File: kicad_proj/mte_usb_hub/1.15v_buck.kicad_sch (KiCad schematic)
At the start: 11 parts

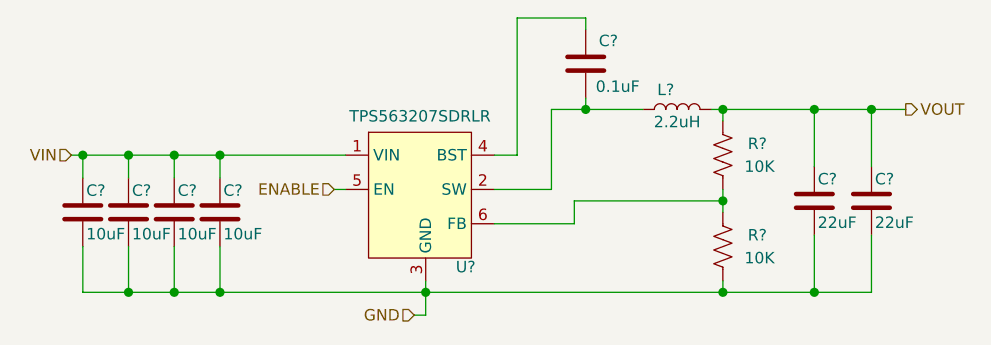
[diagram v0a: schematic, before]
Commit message: Finishes input filter, minor buck changes
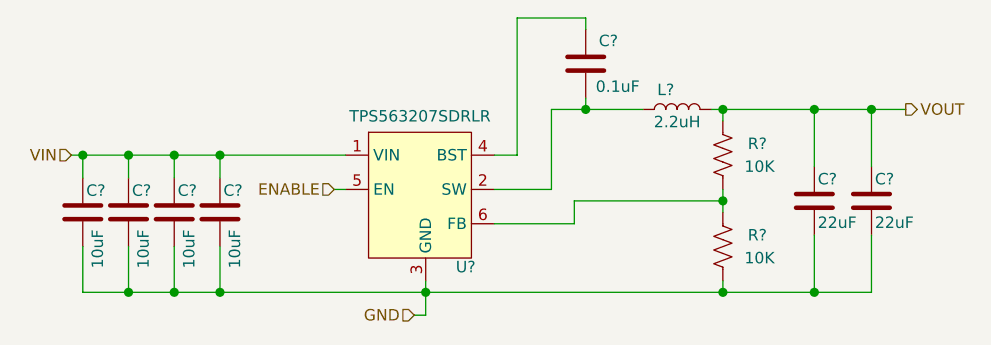
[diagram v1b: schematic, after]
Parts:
- removed C? (x4): C1608X5R1E106M080AC, footprints:CAPACITOR_0603N, symbol mte_usb_hub:C1608X5R1E106M080AC
- added C? (x4): GRM31CR71E106KA12L, footprints:CAPACITOR_1206N, symbol mte_usb_hub:GRM31CR71E106KA12L
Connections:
- net GND: now also C?.2, C?.2, C?.2, C?.2
- net VIN: now also C?.1, C?.1, C?.1, C?.1
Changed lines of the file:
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@@
     (pin "2")
   )
-  (symbol (lib_id "mte_usb_hub:C1608X5R1E106M080AC") (at 20.32 49.53 0) (unit 1)
+  (symbol (lib_id "mte_usb_hub:GRM31CR71E106KA12L") (at 20.32 49.53 0) (unit 1)
     (in_bom yes) (on_board yes)
     (property "Reference" "C?" (id 0) (at 20.7011 47.1106 0)
       (effects (font (size 1.27 1.27)) (justify left))
     )
-    (property "Value" "C1608X5R1E106M080AC" (id 1) (at 20.955 52.07 0)
+    (property "Value" "GRM31CR71E106KA12L" (id 1) (at 20.955 52.07 0)
       (effects (font (size 1.27 1.27)) (justify left) hide)
     )
-    (property "Footprint" "footprints:CAPACITOR_0603N" (id 2) (at 21.2852 53.34 0)
+    (property "Footprint" "footprints:CAPACITOR_1206N" (id 2) (at 21.2852 53.34 0)
       (effects (font (size 1.27 1.27)) hide)
     )
@@
       (effects (font (size 1.27 1.27)) hide)
     )
-    (property "id" "10uF" (id 4) (at 20.7011 51.9493 0)
+    (property "id" "10uF" (id 4) (at 21.9711 55.7593 90)
       (effects (font (size 1.27 1.27)) (justify left))
+    )
+    (property "manf" "Murata Electronics" (id 5) (at 20.32 49.53 0)
+      (effects (font (size 1.27 1.27)) hide)
     )
     (pin "1")
     (pin "2")
   )
-  (symbol (lib_id "mte_usb_hub:C1608X5R1E106M080AC") (at 25.4 49.53 0) (unit 1)
+  (symbol (lib_id "mte_usb_hub:GRM31CR71E106KA12L") (at 25.4 49.53 0) (unit 1)
     (in_bom yes) (on_board yes)
     (property "Reference" "C?" (id 0) (at 25.7811 47.1106 0)
       (effects (font (size 1.27 1.27)) (justify left))
     )
-    (property "Value" "C1608X5R1E106M080AC" (id 1) (at 26.035 52.07 0)
+    (property "Value" "GRM31CR71E106KA12L" (id 1) (at 26.035 52.07 0)
       (effects (font (size 1.27 1.27)) (justify left) hide)
     )
-    (property "Footprint" "footprints:CAPACITOR_0603N" (id 2) (at 26.3652 53.34 0)
+    (property "Footprint" "footprints:CAPACITOR_1206N" (id 2) (at 26.3652 53.34 0)
       (effects (font (size 1.27 1.27)) hide)
     )
@@
       (effects (font (size 1.27 1.27)) hide)
     )
-    (property "id" "10uF" (id 4) (at 25.7811 51.9493 0)
+    (property "id" "10uF" (id 4) (at 27.0511 55.7593 90)
       (effects (font (size 1.27 1.27)) (justify left))
+    )
+    (property "manf" "Murata Electronics" (id 5) (at 25.4 49.53 0)
+      (effects (font (size 1.27 1.27)) hide)
     )
     (pin "1")
     (pin "2")
   )
-  (symbol (lib_id "mte_usb_hub:C1608X5R1E106M080AC") (at 30.48 49.53 0) (unit 1)
+  (symbol (lib_id "mte_usb_hub:GRM31CR71E106KA12L") (at 30.48 49.53 0) (unit 1)
     (in_bom yes) (on_board yes)
     (property "Reference" "C?" (id 0) (at 30.8611 47.1106 0)
       (effects (font (size 1.27 1.27)) (justify left))
     )
-    (property "Value" "C1608X5R1E106M080AC" (id 1) (at 31.115 52.07 0)
+    (property "Value" "GRM31CR71E106KA12L" (id 1) (at 31.115 52.07 0)
       (effects (font (size 1.27 1.27)) (justify left) hide)
     )
-    (property "Footprint" "footprints:CAPACITOR_0603N" (id 2) (at 31.4452 53.34 0)
+    (property "Footprint" "footprints:CAPACITOR_1206N" (id 2) (at 31.4452 53.34 0)
       (effects (font (size 1.27 1.27)) hide)
     )
@@
       (effects (font (size 1.27 1.27)) hide)
     )
-    (property "id" "10uF" (id 4) (at 30.8611 51.9493 0)
+    (property "id" "10uF" (id 4) (at 32.1311 55.7593 90)
       (effects (font (size 1.27 1.27)) (justify left))
+    )
+    (property "manf" "Murata Electronics" (id 5) (at 30.48 49.53 0)
+      (effects (font (size 1.27 1.27)) hide)
     )
     (pin "1")
     (pin "2")
   )
-  (symbol (lib_id "mte_usb_hub:C1608X5R1E106M080AC") (at 35.56 49.53 0) (unit 1)
+  (symbol (lib_id "mte_usb_hub:GRM31CR71E106KA12L") (at 35.56 49.53 0) (unit 1)
     (in_bom yes) (on_board yes)
     (property "Reference" "C?" (id 0) (at 35.9411 47.1106 0)
       (effects (font (size 1.27 1.27)) (justify left))
     )
-    (property "Value" "C1608X5R1E106M080AC" (id 1) (at 36.195 52.07 0)
+    (property "Value" "GRM31CR71E106KA12L" (id 1) (at 36.195 52.07 0)
       (effects (font (size 1.27 1.27)) (justify left) hide)
     )
-    (property "Footprint" "footprints:CAPACITOR_0603N" (id 2) (at 36.5252 53.34 0)
+    (property "Footprint" "footprints:CAPACITOR_1206N" (id 2) (at 36.5252 53.34 0)
       (effects (font (size 1.27 1.27)) hide)
     )
@@
       (effects (font (size 1.27 1.27)) hide)
     )
-    (property "id" "10uF" (id 4) (at 35.9411 51.9493 0)
+    (property "id" "10uF" (id 4) (at 37.2111 55.7593 90)
       (effects (font (size 1.27 1.27)) (justify left))
     )
+    (property "manf" "Murata Electronics" (id 5) (at 35.56 49.53 0)
+      (effects (font (size 1.27 1.27)) hide)
+    )
     (pin "1")

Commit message: Updates input protection, output BC enabled
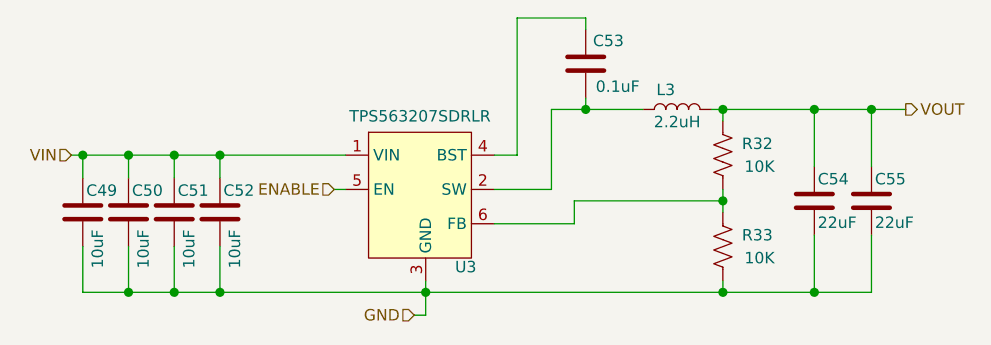
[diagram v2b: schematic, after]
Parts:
- gave numbers to parts that had none: 11
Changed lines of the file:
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@@
-(kicad_sch (version 20210126) (generator eeschema)
+(kicad_sch (version 20210406) (generator eeschema)
   (paper "A4")
   (junction (at 20.32 43.18) (diameter 1.016) (color 0 0 0 0))
@@
   (symbol (lib_id "mte_usb_hub:74405042022") (at 86.36 38.1 90) (unit 1)
     (in_bom yes) (on_board yes)
-    (property "Reference" "L?" (id 0) (at 85.09 35.9218 90))
+    (property "Reference" "L3" (id 0) (at 85.09 35.9218 90))
     (property "Value" "74405042022" (id 1) (at 86.36 36.195 90)
       (effects (font (size 1.27 1.27)) hide)
@@
   (symbol (lib_id "mte_usb_hub:RC0402JR-0710KL") (at 91.44 43.18 0) (unit 1)
     (in_bom yes) (on_board yes)
-    (property "Reference" "R?" (id 0) (at 95.2692 41.91 0))
+    (property "Reference" "R32" (id 0) (at 95.2692 41.91 0))
     (property "Value" "RC0402JR-0710KL" (id 1) (at 88.9 43.18 90)
       (effects (font (size 1.27 1.27)) hide)
@@
   (symbol (lib_id "mte_usb_hub:RC0402JR-0710KL") (at 91.44 53.34 0) (unit 1)
     (in_bom yes) (on_board yes)
-    (property "Reference" "R?" (id 0) (at 95.2692 52.07 0))
+    (property "Reference" "R33" (id 0) (at 95.2692 52.07 0))
     (property "Value" "RC0402JR-0710KL" (id 1) (at 88.9 53.34 90)
       (effects (font (size 1.27 1.27)) hide)
@@
   (symbol (lib_id "mte_usb_hub:GRM31CR71E106KA12L") (at 20.32 49.53 0) (unit 1)
     (in_bom yes) (on_board yes)
-    (property "Reference" "C?" (id 0) (at 20.7011 47.1106 0)
+    (property "Reference" "C49" (id 0) (at 20.7011 47.1106 0)
       (effects (font (size 1.27 1.27)) (justify left))
     )
@@
   (symbol (lib_id "mte_usb_hub:GRM31CR71E106KA12L") (at 25.4 49.53 0) (unit 1)
     (in_bom yes) (on_board yes)
-    (property "Reference" "C?" (id 0) (at 25.7811 47.1106 0)
+    (property "Reference" "C50" (id 0) (at 25.7811 47.1106 0)
       (effects (font (size 1.27 1.27)) (justify left))
     )
@@
   (symbol (lib_id "mte_usb_hub:GRM31CR71E106KA12L") (at 30.48 49.53 0) (unit 1)
     (in_bom yes) (on_board yes)
-    (property "Reference" "C?" (id 0) (at 30.8611 47.1106 0)
+    (property "Reference" "C51" (id 0) (at 30.8611 47.1106 0)
       (effects (font (size 1.27 1.27)) (justify left))
     )
@@
   (symbol (lib_id "mte_usb_hub:GRM31CR71E106KA12L") (at 35.56 49.53 0) (unit 1)
     (in_bom yes) (on_board yes)
-    (property "Reference" "C?" (id 0) (at 35.9411 47.1106 0)
+    (property "Reference" "C52" (id 0) (at 35.9411 47.1106 0)
       (effects (font (size 1.27 1.27)) (justify left))
     )
@@
   (symbol (lib_id "mte_usb_hub:CC0402KRX5R7BB104") (at 76.2 33.02 180) (unit 1)
     (in_bom yes) (on_board yes)
-    (property "Reference" "C?" (id 0) (at 78.7208 30.48 0))
+    (property "Reference" "C53" (id 0) (at 78.7208 30.48 0))
     (property "Value" "CC0402KRX5R7BB104" (id 1) (at 75.565 30.48 0)
       (effects (font (size 1.27 1.27)) (justify left) hide)
@@
   (symbol (lib_id "mte_usb_hub:CL21A226MOCLRNC") (at 101.6 48.26 0) (unit 1)
     (in_bom yes) (on_board yes)
-    (property "Reference" "C?" (id 0) (at 101.9811 45.8406 0)
+    (property "Reference" "C54" (id 0) (at 101.9811 45.8406 0)
       (effects (font (size 1.27 1.27)) (justify left))
     )
@@
   (symbol (lib_id "mte_usb_hub:CL21A226MOCLRNC") (at 107.95 48.26 0) (unit 1)
     (in_bom yes) (on_board yes)
-    (property "Reference" "C?" (id 0) (at 108.3311 45.8406 0)
+    (property "Reference" "C55" (id 0) (at 108.3311 45.8406 0)
       (effects (font (size 1.27 1.27)) (justify left))
     )
@@
   (symbol (lib_id "mte_usb_hub:TPS563207SDRLR") (at 58.42 46.99 0) (unit 1)
     (in_bom yes) (on_board yes)
-    (property "Reference" "U?" (id 0) (at 62.865 55.6063 0))
+    (property "Reference" "U3" (id 0) (at 62.865 55.6063 0))
     (property "Value" "TPS563207SDRLR" (id 1) (at 58.42 46.99 0)
       (effects (font (size 1.27 1.27)) hide)

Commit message: New changes from the livestream
Starts the layout
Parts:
- C49, C50, C51, C52: footprint footprints:CAPACITOR_1206N -> mte_usb_footprints:CAPACITOR_1206N
- C53: footprint footprints:CAPACITOR_0402N -> mte_usb_footprints:CAPACITOR_0402N
- C54, C55: footprint footprints:CAPACITOR_0805N -> mte_usb_footprints:CAPACITOR_0805N
- L3: footprint (none) -> mte_usb_footprints:INDM400X400X200L95X310N
- R32, R33: footprint footprints:RESISTOR_0402N -> mte_usb_footprints:RESISTOR_0402N
- U3: footprint (none) -> mte_usb_footprints:SOL6P50_160X160X60L21N
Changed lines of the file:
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@@
       (effects (font (size 1.27 1.27)) hide)
     )
-    (property "Footprint" "" (id 2) (at 86.36 38.1 0)
+    (property "Footprint" "mte_usb_footprints:INDM400X400X200L95X310N" (id 2) (at 86.36 38.1 0)
       (effects (font (size 1.27 1.27)) hide)
     )
@@
       (effects (font (size 1.27 1.27)) hide)
     )
-    (property "Footprint" "footprints:RESISTOR_0402N" (id 2) (at 92.456 43.434 90)
+    (property "Footprint" "mte_usb_footprints:RESISTOR_0402N" (id 2) (at 92.456 43.434 90)
       (effects (font (size 1.27 1.27)) hide)
     )
@@
       (effects (font (size 1.27 1.27)) hide)
     )
-    (property "Footprint" "footprints:RESISTOR_0402N" (id 2) (at 92.456 53.594 90)
+    (property "Footprint" "mte_usb_footprints:RESISTOR_0402N" (id 2) (at 92.456 53.594 90)
       (effects (font (size 1.27 1.27)) hide)
     )
@@
       (effects (font (size 1.27 1.27)) (justify left) hide)
     )
-    (property "Footprint" "footprints:CAPACITOR_1206N" (id 2) (at 21.2852 53.34 0)
+    (property "Footprint" "mte_usb_footprints:CAPACITOR_1206N" (id 2) (at 21.2852 53.34 0)
       (effects (font (size 1.27 1.27)) hide)
     )
@@
       (effects (font (size 1.27 1.27)) (justify left) hide)
     )
-    (property "Footprint" "footprints:CAPACITOR_1206N" (id 2) (at 26.3652 53.34 0)
+    (property "Footprint" "mte_usb_footprints:CAPACITOR_1206N" (id 2) (at 26.3652 53.34 0)
       (effects (font (size 1.27 1.27)) hide)
     )
@@
       (effects (font (size 1.27 1.27)) (justify left) hide)
     )
-    (property "Footprint" "footprints:CAPACITOR_1206N" (id 2) (at 31.4452 53.34 0)
+    (property "Footprint" "mte_usb_footprints:CAPACITOR_1206N" (id 2) (at 31.4452 53.34 0)
       (effects (font (size 1.27 1.27)) hide)
     )
@@
       (effects (font (size 1.27 1.27)) (justify left) hide)
     )
-    (property "Footprint" "footprints:CAPACITOR_1206N" (id 2) (at 36.5252 53.34 0)
+    (property "Footprint" "mte_usb_footprints:CAPACITOR_1206N" (id 2) (at 36.5252 53.34 0)
       (effects (font (size 1.27 1.27)) hide)
     )
@@
       (effects (font (size 1.27 1.27)) (justify left) hide)
     )
-    (property "Footprint" "footprints:CAPACITOR_0402N" (id 2) (at 75.2348 29.21 0)
+    (property "Footprint" "mte_usb_footprints:CAPACITOR_0402N" (id 2) (at 75.2348 29.21 0)
       (effects (font (size 1.27 1.27)) hide)
     )
@@
       (effects (font (size 1.27 1.27)) (justify left) hide)
     )
-    (property "Footprint" "footprints:CAPACITOR_0805N" (id 2) (at 102.5652 52.07 0)
+    (property "Footprint" "mte_usb_footprints:CAPACITOR_0805N" (id 2) (at 102.5652 52.07 0)
       (effects (font (size 1.27 1.27)) hide)
     )
@@
       (effects (font (size 1.27 1.27)) (justify left) hide)
     )
-    (property "Footprint" "footprints:CAPACITOR_0805N" (id 2) (at 108.9152 52.07 0)
+    (property "Footprint" "mte_usb_footprints:CAPACITOR_0805N" (id 2) (at 108.9152 52.07 0)
       (effects (font (size 1.27 1.27)) hide)
     )
@@
       (effects (font (size 1.27 1.27)) hide)
     )
-    (property "Footprint" "" (id 2) (at 58.42 46.99 0)
-      (effects (font (size 1.27 1.27)) hide)
-    )
+    (property "Footprint" "mte_usb_footprints:SOL6P50_160X160X60L21N" (id 2) (at 58.42 46.99 0)
+      (effects (font (size 1.27 1.27)) hide)
+    )
